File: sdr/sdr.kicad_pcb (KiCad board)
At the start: 4 copper layers, 85 x 53 mm, 60 parts, among them J1 USB_C_Receptacle_USB2.0, J2 SWD, J3 Conn_Coaxial, Q1 AO3400A, Q2 AO3401A, Q3 AO3400A, Q4 AO3401A, SW1 RESET, SW2 KEY, U1 AMS1117-3.3, U2 MS5351M, U3 LM4871M/TR_C383075, U4 CH32V305RBT6, U5 BGA2817, U6 NC7SVU04P5X, U7 NC7SVU04P5X, Y1 25MHz, Y2 25MHz

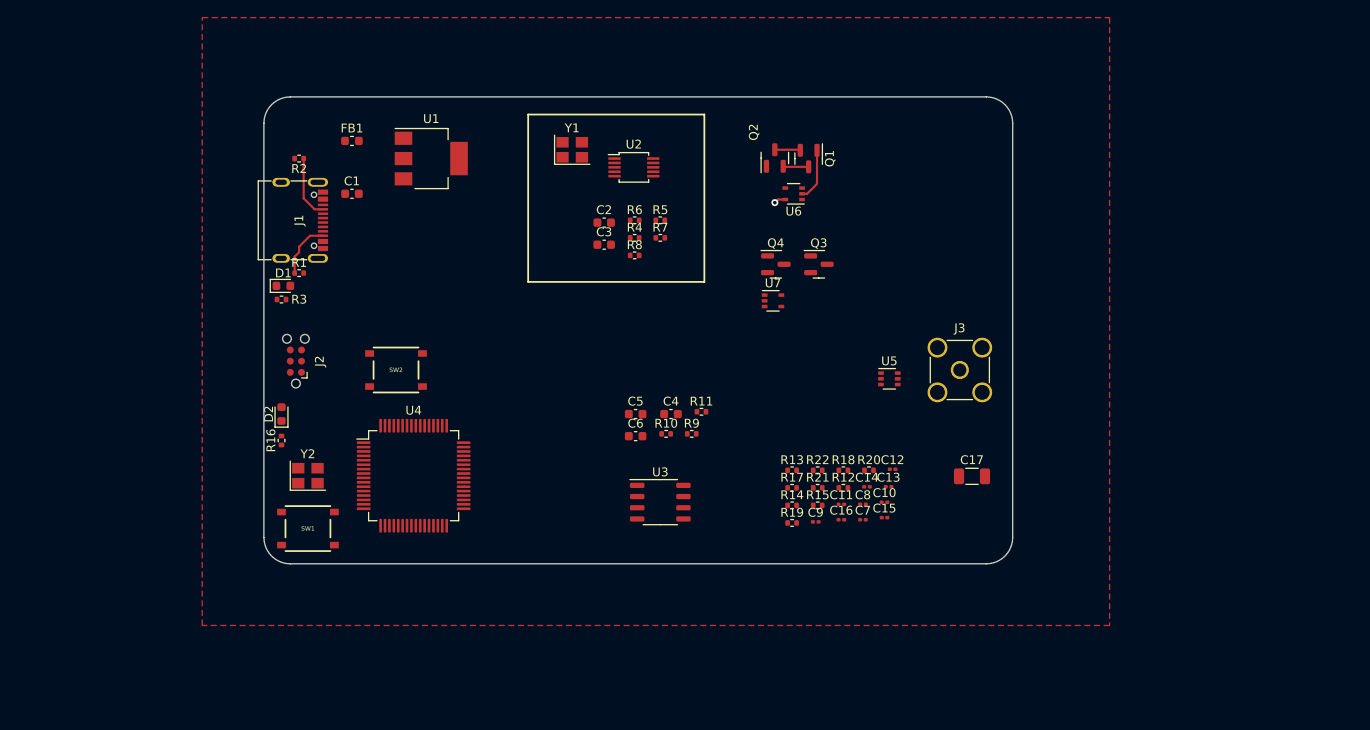
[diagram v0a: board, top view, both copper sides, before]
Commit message: Added ST-link 6-pin 0.1 programming header
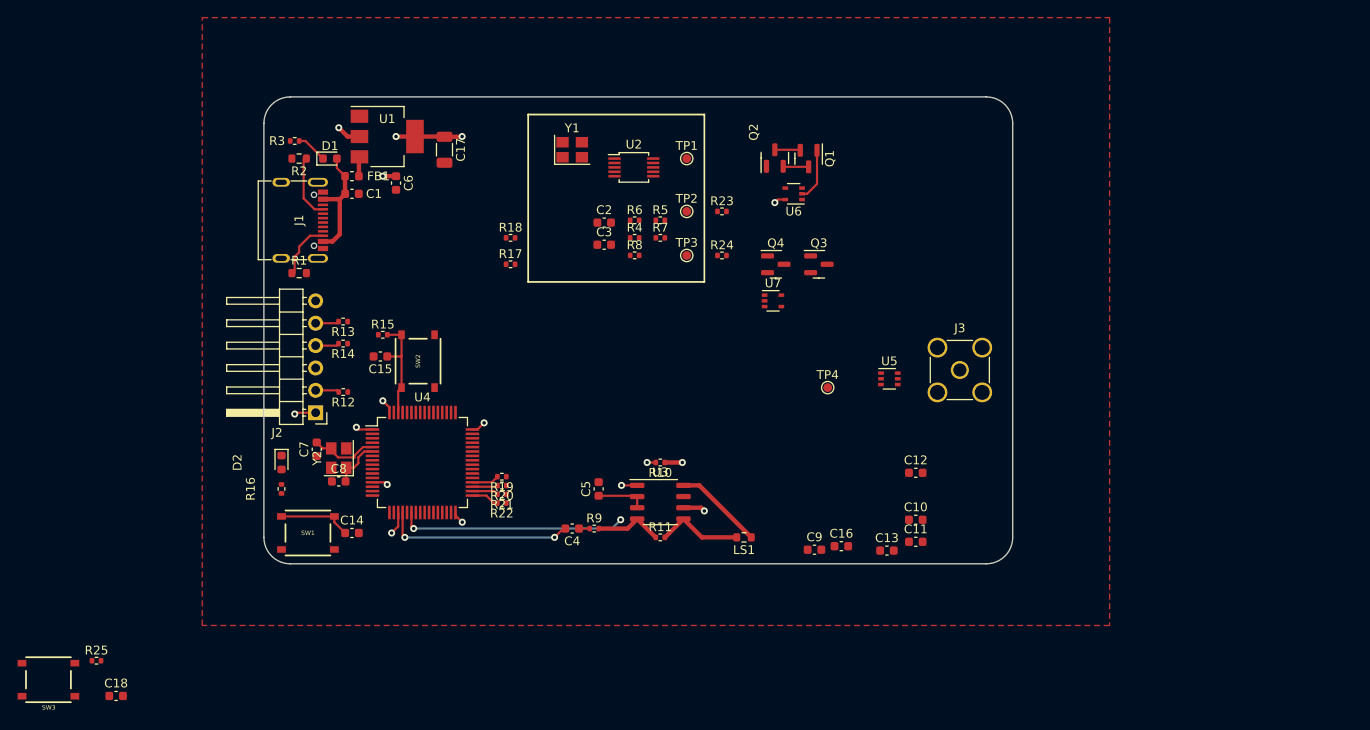
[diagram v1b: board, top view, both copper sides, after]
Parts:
- added C18: 100n, Capacitor_SMD:C_0603_1608Metric, F.Cu at (102.2, 132.0)
- added LS1: Speaker, Resistor_SMD:R_0603_1608Metric, F.Cu at (173.5, 114.0)
- added R23: 0, Resistor_SMD:R_0402_1005Metric, F.Cu at (171.0, 77.0)
- added R24: 0, Resistor_SMD:R_0402_1005Metric, F.Cu at (171.0, 82.0)
- added R25: 10k, Resistor_SMD:R_0402_1005Metric, F.Cu at (100.0, 128.0)
- added SW3: PTT, ZL4AA:TS-1187A-B-A-B, F.Cu at (94.5, 130.2)
- added TP1: VFO, TestPoint:TestPoint_Pad_D1.0mm, F.Cu at (167.0, 71.0)
- added TP2: I, TestPoint:TestPoint_Pad_D1.0mm, F.Cu at (167.0, 77.0)
- added TP3: Q, TestPoint:TestPoint_Pad_D1.0mm, F.Cu at (167.0, 82.0)
- added TP4: RF_IN, TestPoint:TestPoint_Pad_D1.0mm, F.Cu at (183.0, 97.0)
- C10, C11, C12, C13, C14, C15, C16, C7, C8, C9: footprint Capacitor_SMD:C_0201_0603Metric -> Capacitor_SMD:C_0603_1608Metric
- J2: value SWD -> Conn_01x06; footprint Connector:Tag-Connect_TC2030-IDC-NL_2x03_P1.27mm_Vertical -> Connector_PinHeader_2.54mm:PinHeader_1x06_P2.54mm_Horizontal
- R1, R2: footprint Resistor_SMD:R_0402_1005Metric -> Resistor_SMD:R_0603_1608Metric
- moved C17 70.4 mm to (139.5, 70.0), turned to -90 degrees
- moved C7 62.5 mm to (125.0, 104.0), turned to 90 degrees
- moved C15 60.1 mm to (132.2, 93.5), turned to 180 degrees
- moved C8 59.6 mm to (127.5, 107.6)
- moved C14 58.7 mm to (129.0, 113.5)
- moved R12 57.8 mm to (128.0, 97.5), turned to 180 degrees
- moved R14 54.2 mm to (128.0, 92.0), turned to 180 degrees
- moved R13 53.7 mm to (128.0, 89.5), turned to 180 degrees
- moved R15 53.0 mm to (132.5, 91.0)
- moved R18 46.1 mm to (147.0, 80.0)
- moved R20 41.7 mm to (146.0, 108.1), turned to 180 degrees
- moved R17 40.8 mm to (147.0, 83.0)
- moved C6 39.6 mm to (134.0, 73.8), turned to -90 degrees
- moved R22 36.1 mm to (146.0, 110.1), turned to 180 degrees
- moved R21 35.9 mm to (146.0, 109.1), turned to 180 degrees
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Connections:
- D1 pad 2: +5V -> Net-(C1-Pad1)
- J2 pad 2: Net-(J2-Pad2) -> Net-(R12-Pad2)
- J2 pad 3: Net-(J2-Pad3) -> GND
- J2 pad 4: Net-(J2-Pad4) -> Net-(R14-Pad2)
- J2 pad 5: GND -> Net-(R13-Pad2)
- Q1 pad 1: /Freq Synthesizer/LO_I -> /Mixer I/LO
- Q3 pad 1: /Freq Synthesizer/LO_Q -> /Mixer Q/LO
- R10 pad 2: Net-(R10-Pad2) -> /Audio Output/SHUTDOWN
- R12 pad 2: Net-(J2-Pad4) -> Net-(R12-Pad2)
- R13 pad 2: Net-(J2-Pad3) -> Net-(R13-Pad2)
- R14 pad 2: Net-(J2-Pad2) -> Net-(R14-Pad2)
- R17 pad 2: /CPU/I2C_SCL -> /CPU/I2C_SDA
- R4 pad 2: /CPU/I2C_SCL -> /CPU/I2C_SDA
- U2 pad 5: /CPU/I2C_SCL -> /CPU/I2C_SDA
- U3 pad 1: Net-(R10-Pad2) -> /Audio Output/SHUTDOWN
- U4 pad 20: /CPU/BB_I -> /Audio Output/AUDIO
- U4 pad 22: unconnected-(U4-Pad22) -> /Audio Output/SHUTDOWN
- U4 pad 39: unconnected-(U4-Pad39) -> PTT
- U6 pad 2: /Freq Synthesizer/LO_I -> /Mixer I/LO
- U7 pad 2: /Freq Synthesizer/LO_Q -> /Mixer Q/LO
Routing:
- net +5V: track 0.00 -> 116.9 mm, vias 0 -> 3
- net /Audio Output/SHUTDOWN: track 0.00 -> 37.7 mm, vias 0 -> 4
- net +3.3V: track 1.33 -> 25.8 mm, vias 1 -> 11
- net /Audio Output/AUDIO: track 0.00 -> 21.6 mm, vias 0 -> 2
- net Net-(C1-Pad1): track 0.00 -> 13.4 mm
- net KEY: track 0.00 -> 12.3 mm
- net Net-(LS1-Pad1): track 0.00 -> 10.1 mm
- net Net-(LS1-Pad2): track 0.00 -> 9.90 mm
- net NRST: track 0.00 -> 8.38 mm
- net Net-(R11-Pad1): track 0.00 -> 7.80 mm
- net Net-(C7-Pad2): track 0.00 -> 7.78 mm
- net /Mixer I/LO: track 0.00 -> 5.98 mm
- net /Freq Synthesizer/LO_I: track 5.98 -> 0.00 mm
- net Net-(C8-Pad2): track 0.00 -> 5.71 mm
- net Net-(C5-Pad1): track 0.00 -> 5.68 mm
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
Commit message: Tighten up design layout.
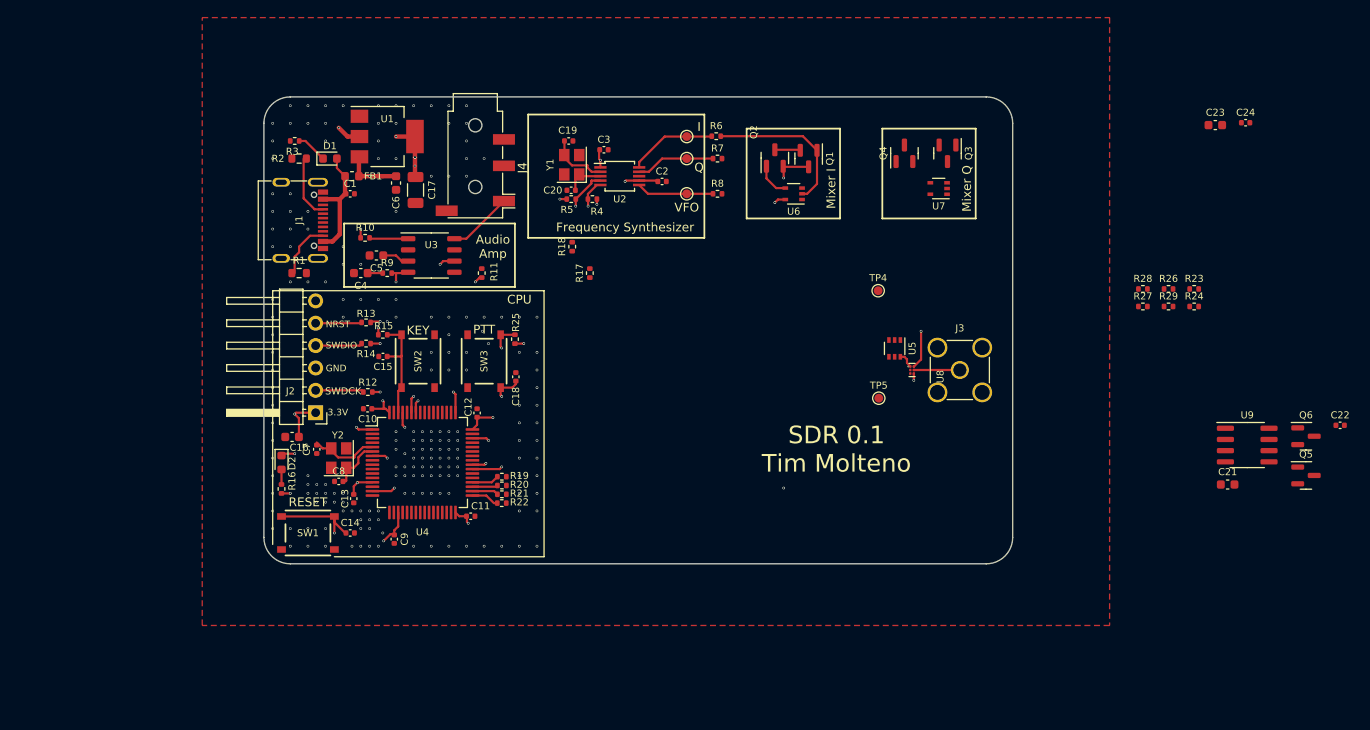
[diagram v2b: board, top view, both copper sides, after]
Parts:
- removed LS1: Speaker, Resistor_SMD:R_0603_1608Metric
- added C19: 2p, Capacitor_SMD:C_0402_1005Metric, F.Cu at (153.6, 69.0)
- added C20: 2p, Capacitor_SMD:C_0402_1005Metric, F.Cu at (153.9, 74.6)
- added C21: 1u, Capacitor_SMD:C_0603_1608Metric, F.Cu at (228.4, 108.0)
- added C22: 100n, Capacitor_SMD:C_0402_1005Metric, F.Cu at (241.2, 101.3)
- added C23: 1u, Capacitor_SMD:C_0603_1608Metric, F.Cu at (227.0, 67.2)
- added C24: 100n, Capacitor_SMD:C_0402_1005Metric, F.Cu at (230.4, 66.9)
- added J4: AudioJack4, Connector_Audio:Jack_3.5mm_PJ320D_Horizontal, F.Cu at (143.0, 72.0)
- added Q5: AO3400A, Package_TO_SOT_SMD:SOT-23, F.Cu at (237.3, 107.0)
- added Q6: AO3401A, Package_TO_SOT_SMD:SOT-23, F.Cu at (237.3, 102.5)
- added R26: 50, Resistor_SMD:R_0402_1005Metric, F.Cu at (221.7, 85.8)
- added R27: 24, Resistor_SMD:R_0402_1005Metric, F.Cu at (218.8, 87.8)
- added R28: 100, Resistor_SMD:R_0402_1005Metric, F.Cu at (218.8, 85.8)
- added R29: 4.7, Resistor_SMD:R_0402_1005Metric, F.Cu at (221.7, 87.8)
- added TP5: RF_OUT, TestPoint:TestPoint_Pad_D1.0mm, F.Cu at (188.8, 98.2)
- added U8: FM1630C, ZL4AA:DFN-6_L1.1-W0.7-P0.40-BL, F.Cu at (192.6, 95.0)
- added U9: AD8001AR, Package_SO:SOIC-8_3.9x4.9mm_P1.27mm, F.Cu at (230.6, 103.5)
- C1, C10, C11, C12, C13, C14, C15, C18, C2, C3, C7, C8, C9: footprint Capacitor_SMD:C_0603_1608Metric -> Capacitor_SMD:C_0402_1005Metric
- C16: value 500n -> 470n
- R23: value 0 -> 4.7
- R24: value 0 -> 50
- R3: value 500 -> 470
- TP2: value I -> Q
- TP3: value Q -> I
- moved C16 63.6 mm to (122.2, 102.6), turned to 180 degrees
- moved C10 63.5 mm to (130.8, 99.4), turned to 180 degrees
- moved SW3 61.3 mm to (144.0, 94.0), turned to 90 degrees
- moved C13 60.8 mm to (129.2, 109.6), turned to -90 degrees
- moved R25 59.9 mm to (147.5, 91.5), turned to 90 degrees
- moved C18 58.1 mm to (147.6, 95.8), turned to 90 degrees
- moved R23 54.3 mm to (224.6, 85.8)
- moved R24 53.9 mm to (224.6, 87.8)
- moved C11 50.6 mm to (142.5, 111.6)
- moved C12 50.3 mm to (143.2, 99.9), turned to 90 degrees
- moved C9 47.7 mm to (133.8, 114.2), turned to -90 degrees
- moved R10 42.1 mm to (130.5, 80.0), turned to 0 degrees
- moved U3 38.2 mm to (138.0, 82.0)
- moved C4 37.6 mm to (130.0, 84.0)
- moved R9 37.3 mm to (133.0, 84.0)
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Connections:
- net Net-(R12-Pad1) renamed SWCLK
- net Net-(R14-Pad1) renamed SWDIO
- Q1 pad 1: /Mixer I/LO -> /Freq Synthesizer/LO_I
- Q3 pad 1: /Mixer Q/LO -> /Freq Synthesizer/LO_Q
- R11 pad 2: Net-(LS1-Pad2) -> GND
- R23 pad 1: /Mixer I/LO -> /TX Amplifier/RF_OUT
- R23 pad 2: /Freq Synthesizer/LO_I -> Net-(Q6-Pad3)
- R24 pad 1: /Freq Synthesizer/LO_Q -> Net-(R24-Pad1)
- R24 pad 2: /Mixer Q/LO -> /TX Amplifier/I_IN
- R4 pad 1: +3.3V -> /CPU/I2C_SDA
- R4 pad 2: /CPU/I2C_SDA -> +3.3V
- TP1 pad 1: /Freq Synthesizer/VFO -> Net-(R8-Pad1)
- TP2 pad 1: /Freq Synthesizer/LO_I -> Net-(R7-Pad1)
- TP3 pad 1: /Freq Synthesizer/LO_Q -> Net-(R6-Pad1)
- U3 pad 5: Net-(LS1-Pad2) -> GND
- U3 pad 8: Net-(LS1-Pad1) -> LEFT
- U4 pad 40: unconnected-(U4-Pad40) -> RX_EN
- U5 pad 6: Net-(J3-Pad1) -> Net-(U5-Pad6)
- U6 pad 2: /Mixer I/LO -> /Freq Synthesizer/LO_I
- U7 pad 2: /Mixer Q/LO -> /Freq Synthesizer/LO_Q
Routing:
- net +5V: track 116.9 -> 28.5 mm, vias 3 -> 4
- net /CPU/INPUT_I: track 2.91 -> 86.1 mm, vias 0 -> 3
- net RX_EN: track 0.00 -> 70.9 mm, vias 0 -> 3
- net NRST: track 8.38 -> 43.5 mm, vias 0 -> 5
- net /Audio Output/SHUTDOWN: track 37.7 -> 4.41 mm, vias 4 -> 0
- net SWDIO: track 0.00 -> 26.3 mm, vias 0 -> 3
- net PTT: track 0.00 -> 23.4 mm, vias 0 -> 3
- net /Audio Output/AUDIO: track 21.6 -> 0.00 mm, vias 2 -> 0
- net +3.3V: track 25.8 -> 44.6 mm, vias 11 -> 21
- net LED: track 0.00 -> 18.6 mm, vias 0 -> 3
- net /Freq Synthesizer/LO_I: track 0.00 -> 17.6 mm
- net SWCLK: track 0.00 -> 11.6 mm, vias 0 -> 2
- net Net-(LS1-Pad1): track 10.1 -> 0.00 mm
- net Net-(R6-Pad1): track 0.00 -> 10.00 mm
- net Net-(LS1-Pad2): track 9.90 -> 0.00 mm
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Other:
- copper layers 4 -> 6
- board text added: "3.3V"
- board text added: "Audio Amp"
- board text added: "CPU"
- board text added: "Frequency Synthesizer"
- board text added: "GND"
- board text added: "Mixer I"
- board text added: "Mixer Q"
- board text added: "NRST"
- board text added: "SDR 0.1 Tim Molteno"
- board text added: "SWDCK"
- board text added: "SWDIO"

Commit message: Many fixes. Updated mixers to use the analog switches rather than discretes.
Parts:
- removed Q1, Q3: AO3400A, Package_TO_SOT_SMD:SOT-23
- removed Q2, Q4: AO3401A, Package_TO_SOT_SMD:SOT-23
- added R32: 1, Resistor_SMD:R_0402_1005Metric, F.Cu at (174.0, 100.0)
- added U10: BGA2817, Package_TO_SOT_SMD:SOT-363_SC-70-6, F.Cu at (184.8, 90.0)
- added U11: 74LVC1G66, Package_TO_SOT_SMD:SOT-353_SC-70-5, F.Cu at (176.8, 70.2)
- added U12: 74LVC1G66, Package_TO_SOT_SMD:SOT-353_SC-70-5, F.Cu at (167.8, 93.8)
- added U13: 74LVC1G66, Package_TO_SOT_SMD:SOT-353_SC-70-5, F.Cu at (162.5, 100.9)
- added U14: 74LVC1G66, Package_TO_SOT_SMD:SOT-353_SC-70-5, F.Cu at (166.8, 100.9)
- R24, R26: value 50 -> 120
- R27: value 24 -> 220
- U6: value NC7SVU04P5X -> NC7SB3157L6X; footprint Package_TO_SOT_SMD:SOT-353_SC-70-5 -> Package_SON:Fairchild_MicroPak-6_1.0x1.45mm_P0.5mm
- U7: value NC7SVU04P5X -> 74LVC1G66
- moved U6 30.4 mm to (150.0, 83.5)
- moved U7 19.1 mm to (176.5, 75.0)
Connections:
- R11 pad 2: GND -> Net-(R11-Pad2)
- R27 pad 2: Net-(R24-Pad1) -> V_BIAS
- TP4 pad 1: /Mixer I/RF -> Net-(TP4-Pad1)
- U3 pad 5: GND -> Net-(R11-Pad2)
- U4 pad 15: /CPU/INPUT_I -> /CPU/ADC_I
- U4 pad 16: /CPU/INPUT_Q -> /CPU/ADC_Q
- U4 pad 20: /Audio Output/AUDIO -> /CPU/DAC_I
- U4 pad 21: /CPU/BB_Q -> /CPU/DAC_Q
- U5 pad 3: /Mixer I/RF -> Net-(TP4-Pad1)
- U6 pad 1: unconnected-(U6-Pad1) -> /Audio Output/AUDIO
- U6 pad 2: /Freq Synthesizer/LO_I -> unconnected-(U6-Pad2)
- U6 pad 3: GND -> /Tx Mixers/BB_I
- U6 pad 4: Net-(Q2-Pad1) -> /CPU/DAC_I
- U6 pad 5: +3.3V -> unconnected-(U6-Pad5)
- U7 pad 1: unconnected-(U7-Pad1) -> /Mixer I/RF
- U7 pad 2: /Freq Synthesizer/LO_Q -> /CPU/ADC_I
- U7 pad 4: Net-(Q4-Pad1) -> /Freq Synthesizer/LO_I
- U9 pad 2: GND -> Net-(R24-Pad1)
- U9 pad 3: Net-(R24-Pad1) -> V_BIAS
- U9 pad 7: +5V -> +5P
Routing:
- net /CPU/INPUT_I: track 86.1 -> 0.00 mm, vias 3 -> 0
- net /CPU/ADC_I: track 0.00 -> 82.0 mm, vias 0 -> 2
- net /Freq Synthesizer/LO_I: track 17.6 -> 0.00 mm
- net Net-(Q2-Pad1): track 3.97 -> 0.00 mm
- net /Mixer I/RF: track 2.82 -> 0.00 mm
- net +3.3V: track 44.6 -> 43.3 mm, vias 21 -> 20
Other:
- board text added: "RX Mixer"
- board text added: "TX Mixer"
- board text removed: "Mixer I"
- board text removed: "Mixer Q"

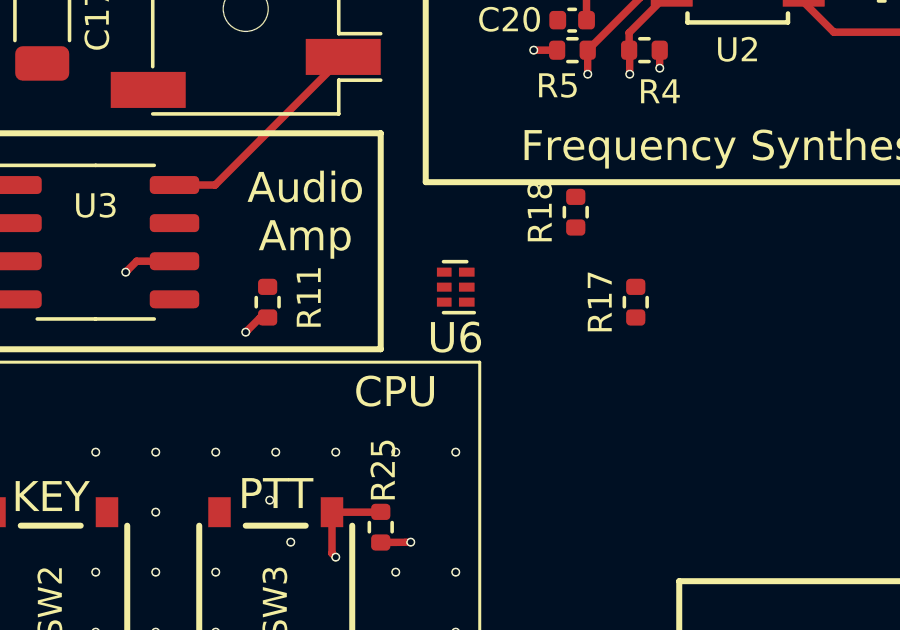
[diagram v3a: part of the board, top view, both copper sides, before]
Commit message: Update to KiCAD 7
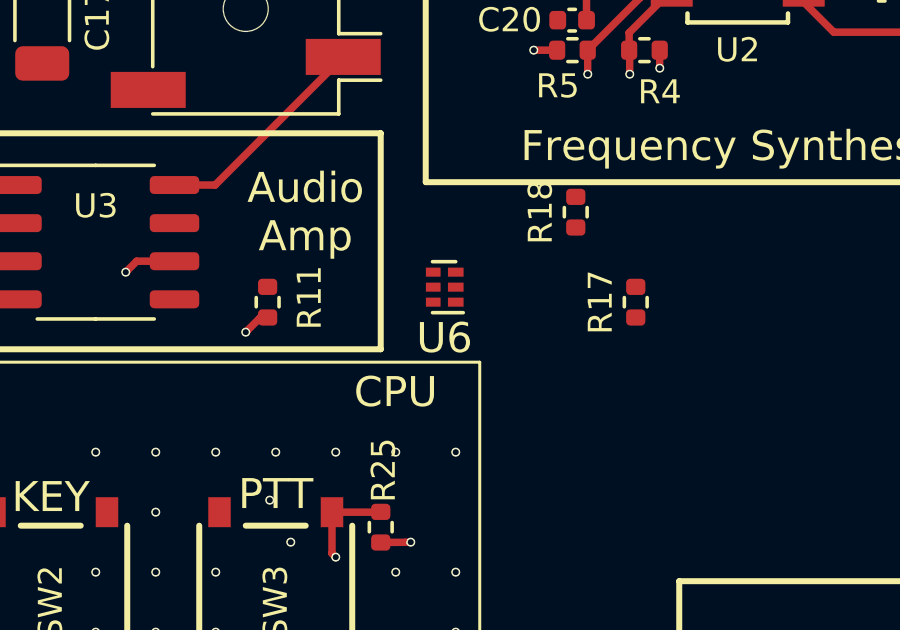
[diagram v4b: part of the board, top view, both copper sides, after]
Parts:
- moved U6 0.37 mm to (149.6, 83.5)

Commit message: Complete layout
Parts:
- removed R26: 120, Resistor_SMD:R_0402_1005Metric
- removed U6: NC7SB3157L6X, Package_SON:Fairchild_MicroPak-6_1.0x1.45mm_P0.5mm
- added C25: 0.5pF, Capacitor_SMD:C_0402_1005Metric, F.Cu at (190.2, 96.2)
- added C26: 100n, Capacitor_SMD:C_0402_1005Metric, F.Cu at (181.5, 91.8)
- added C27: 1n, Capacitor_SMD:C_0402_1005Metric, F.Cu at (181.8, 95.2)
- added C28: 10n, Capacitor_SMD:C_0402_1005Metric, F.Cu at (173.5, 76.0)
- added C29: 10n, Capacitor_SMD:C_0402_1005Metric, F.Cu at (173.5, 71.0)
- added C30: 10n, Capacitor_SMD:C_0402_1005Metric, F.Cu at (158.0, 111.0)
- added R30: 470, Resistor_SMD:R_0402_1005Metric, F.Cu at (186.7, 102.3)
- added R31: 470, Resistor_SMD:R_0402_1005Metric, F.Cu at (189.0, 102.2)
- added R33: 47, Resistor_SMD:R_0402_1005Metric, F.Cu at (155.2, 111.0)
- added R34: 47, Resistor_SMD:R_0402_1005Metric, F.Cu at (155.2, 112.2)
- added R35: 0, Resistor_SMD:R_0402_1005Metric, F.Cu at (165.0, 109.0)
- added TP6: TMIX, TestPoint:TestPoint_Keystone_5015_Micro-Minature, F.Cu at (162.0, 109.0)
- TP1, TP2, TP3: footprint TestPoint:TestPoint_Pad_D1.0mm -> TestPoint:TestPoint_Keystone_5015_Micro-Minature
- TP4: value RF_IN -> RX; footprint TestPoint:TestPoint_Pad_D1.0mm -> TestPoint:TestPoint_Keystone_5015_Micro-Minature
- TP5: value RF_OUT -> TX; footprint TestPoint:TestPoint_Pad_D1.0mm -> TestPoint:TestPoint_Keystone_5015_Micro-Minature
- moved C24 84.6 mm to (156.0, 107.0)
- moved C23 83.5 mm to (157.7, 113.8)
- moved C22 62.3 mm to (180.2, 88.2), turned to -90 degrees
- moved Q5 56.6 mm to (183.7, 88.7), turned to -90 degrees
- moved C21 52.9 mm to (177.0, 95.5), turned to -90 degrees
- moved Q6 50.2 mm to (189.1, 88.7)
- moved U9 45.6 mm to (185.6, 96.2), turned to 90 degrees
- moved R24 42.3 mm to (185.0, 102.8), turned to -90 degrees
- moved R23 36.3 mm to (188.3, 85.0)
- moved R29 36.0 mm to (185.8, 84.9)
- moved R28 32.6 mm to (186.2, 88.2), turned to 90 degrees
- moved R27 28.6 mm to (191.5, 96.2), turned to -90 degrees
- moved U12 20.3 mm to (154.4, 109.1)
- moved U10 19.6 mm to (190.1, 71.2), turned to -90 degrees
- moved TP5 18.3 mm to (187.5, 80.0)
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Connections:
- R24 pad 2: /TX Amplifier/I_IN -> /TX Amplifier/RF_IN
- U12 pad 1: /Tx Mixers/BB_I -> /Audio Output/AUDIO
- U12 pad 4: /Tx Mixers/LO_I -> /Freq Synthesizer/LO_I
- U13 pad 4: /Tx Mixers/LO_Q -> /Freq Synthesizer/LO_Q
- U4 pad 20: /CPU/DAC_I -> /Audio Output/AUDIO
- U4 pad 41: unconnected-(U4-PA8-Pad41) -> TXMIX_EN
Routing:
- net /CPU/ADC_Q: track 0.00 -> 80.0 mm, vias 0 -> 3
- net /Freq Synthesizer/LO_Q: track 0.00 -> 64.5 mm, vias 0 -> 2
- net /Freq Synthesizer/LO_I: track 0.00 -> 61.3 mm, vias 0 -> 3
- net /Audio Output/AUDIO: track 0.00 -> 58.4 mm, vias 0 -> 4
- net Net-(U4-PB7/USB2DP): track 1.93 -> 37.6 mm, vias 1 -> 3
- net Net-(U4-PB6/USB2DM): track 1.43 -> 35.5 mm, vias 1 -> 3
- net /Audio Output/SHUTDOWN: track 4.41 -> 37.4 mm, vias 0 -> 2
- net /TX Amplifier/RF_IN: track 0.00 -> 22.7 mm
- net /CPU/DAC_Q: track 0.00 -> 20.7 mm, vias 0 -> 2
- net /Mixer I/RF: track 0.00 -> 19.5 mm
- net +5P: track 0.00 -> 18.9 mm, vias 0 -> 2
- net TXMIX_EN: track 0.00 -> 18.0 mm, vias 0 -> 2
- net RX_EN: track 70.9 -> 88.3 mm, vias 3 -> 4
- net /TX Amplifier/RF_OUT: track 0.00 -> 12.8 mm
- net +5V: track 28.5 -> 15.9 mm, vias 4 -> 8
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- added copper zone on In4.Cu, net +5V
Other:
- board text added: "Power Amp"
